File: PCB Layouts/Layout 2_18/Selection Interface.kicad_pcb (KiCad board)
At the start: 4 copper layers, 110 x 90 mm, 132 parts

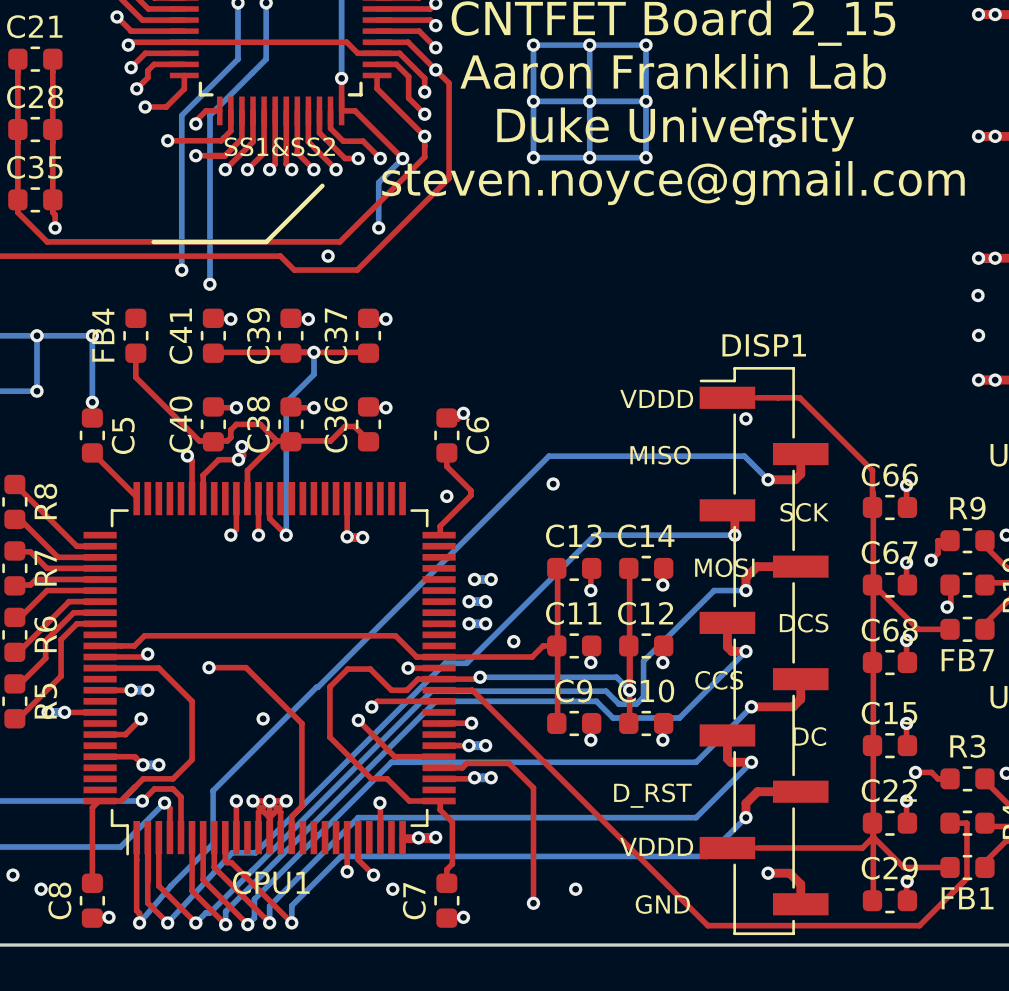
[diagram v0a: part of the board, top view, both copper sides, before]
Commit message: Removed display header from layout 2_18
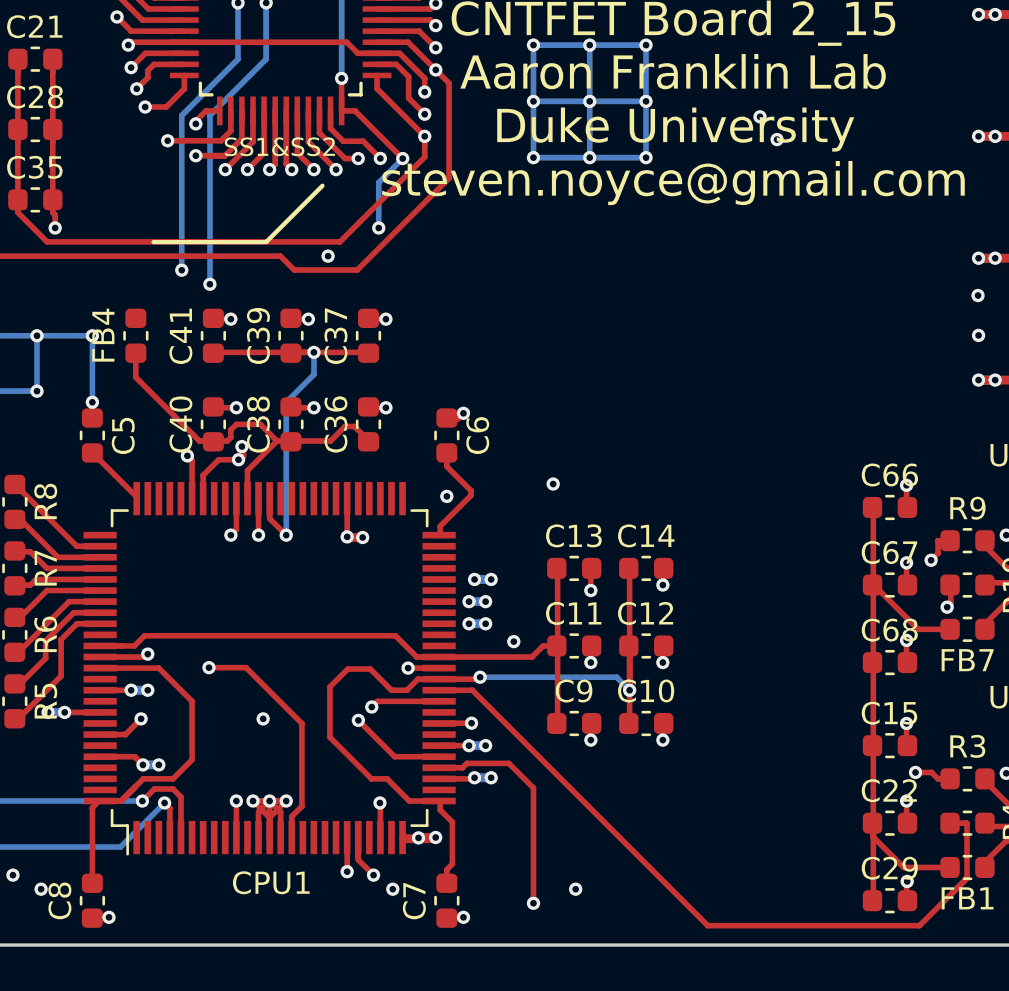
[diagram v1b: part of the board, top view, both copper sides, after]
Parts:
- removed DISP1: Conn_01x10, Connector_PinHeader_2.54mm:PinHeader_1x10_P2.54mm_Vertical_SMD_Pin1Left
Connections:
- CPU1 pad 1: DisplayMISO -> Net-(CPU1-Pad1)
- CPU1 pad 2: DisplaySCK -> Net-(CPU1-Pad2)
- CPU1 pad 3: DisplayMOSI -> Net-(CPU1-Pad3)
- CPU1 pad 6: DisplayCS -> Net-(CPU1-Pad6)
- CPU1 pad 7: CardCS -> Net-(CPU1-Pad7)
- CPU1 pad 8: DisplayDataOrCommand -> Net-(CPU1-Pad8)
- CPU1 pad 9: DisplayReset -> Net-(CPU1-Pad9)
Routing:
- net DisplayMISO: track 45.4 -> 0.00 mm, vias 2 -> 0
- net DisplaySCK: track 40.3 -> 0.00 mm, vias 2 -> 0
- net DisplayMOSI: track 40.3 -> 0.00 mm, vias 2 -> 0
- net DisplayCS: track 36.1 -> 0.00 mm, vias 2 -> 0
- net CardCS: track 35.3 -> 0.00 mm, vias 2 -> 0
- net DisplayDataOrCommand: track 32.2 -> 0.00 mm, vias 2 -> 0
- net DisplayReset: track 31.4 -> 0.00 mm, vias 2 -> 0
- net VDDD: track 281.8 -> 267.5 mm, vias 16 -> 15
- net GND: track 597.7 -> 595.2 mm, vias 189 -> 188
- net SolutionGate_Socket: track 94.1 -> 95.5 mm
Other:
- board text removed: "CCS"
- board text removed: "DC"
- board text removed: "DCS"
- board text removed: "D_RST"
- board text removed: "MISO"
- board text removed: "MOSI"
- board text removed: "SCK"

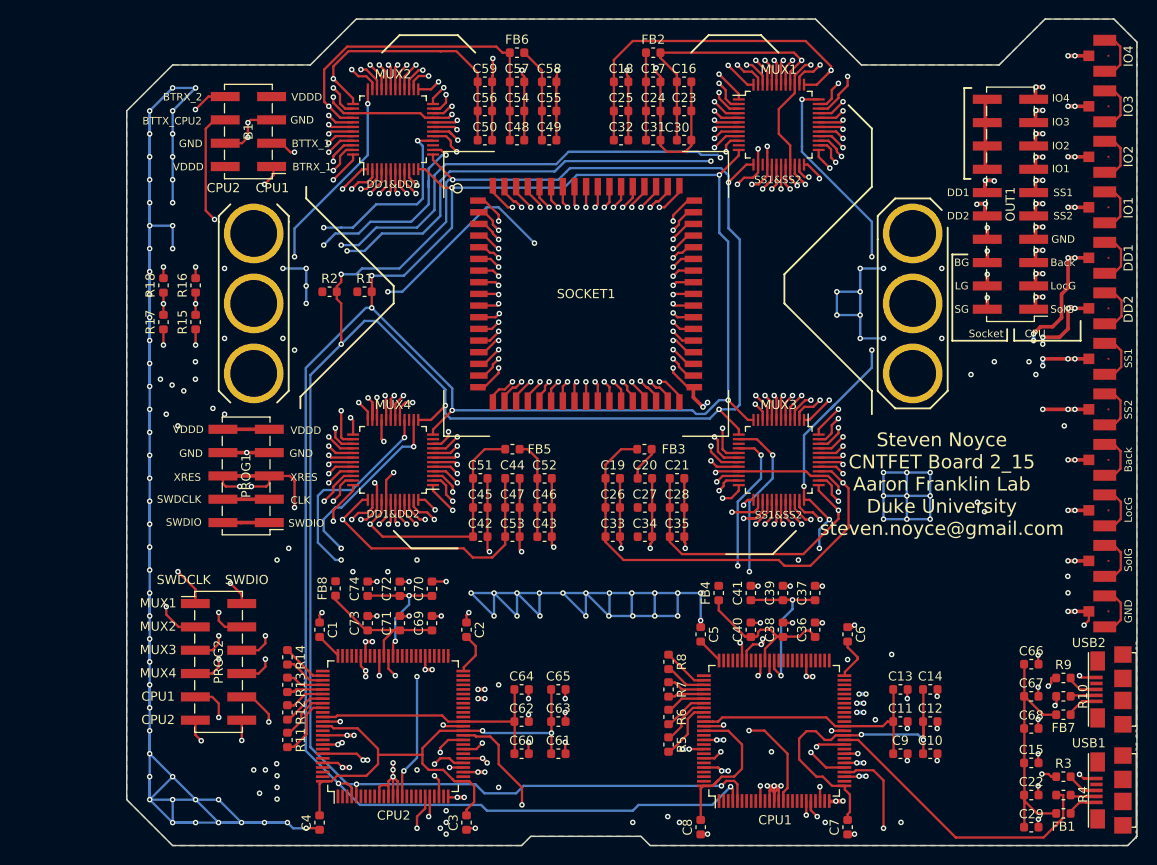
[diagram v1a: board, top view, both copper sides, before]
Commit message: Removed secondary master processor (CPU2) from Layout 2_18
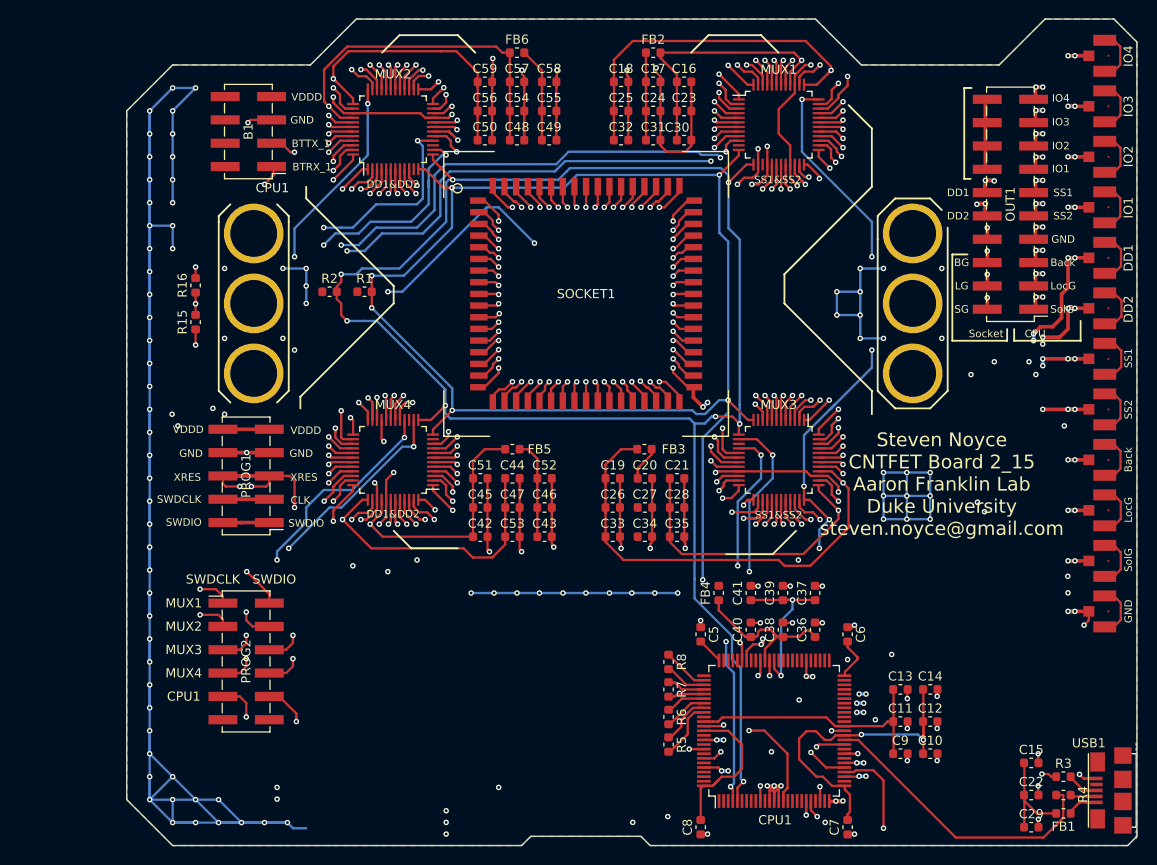
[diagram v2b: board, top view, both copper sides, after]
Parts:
- removed C1, C2, C3, C4, C64, C65, C68, C73, C74: 0.1uF, Capacitor_SMD:C_0603_1608Metric
- removed C60, C61, C66, C69, C70: 47uF, Capacitor_SMD:C_0603_1608Metric
- removed C62, C63, C67, C71, C72: 1uF, Capacitor_SMD:C_0603_1608Metric
- removed CPU2: CY8C58_(100_TQFP), Package_QFP:TQFP-100_14x14mm_P0.5mm
- removed FB7, FB8, R11, R12, R13, R14: R, Resistor_SMD:R_0603_1608Metric
- removed R10, R9: 22R, Resistor_SMD:R_0603_1608Metric
- removed R17: 1k, Resistor_SMD:R_0603_1608Metric
- removed R18: 2k, Resistor_SMD:R_0603_1608Metric
- removed USB2: USB_2.0_B, Custom_Footprint_Library:Micro_USB_2.0_B_SMD(10118192-0001LF)
- moved PROG2 3.00 mm to (163.0, 139.9)
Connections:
- B1 pad 2: VDDD -> Net-(B1-Pad2)
- B1 pad 4: GND -> Net-(B1-Pad4)
- B1 pad 6: BT2_TX -> Net-(B1-Pad6)
- B1 pad 8: BT2_RXR -> Net-(B1-Pad8)
- PROG2 pad 11: SWDCLK6 -> Net-(PROG2-Pad11)
- PROG2 pad 12: SWDIO6 -> Net-(PROG2-Pad12)
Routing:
- net BT2_TX: track 105.1 -> 0.00 mm, vias 5 -> 0
- net GND: track 595.2 -> 493.4 mm, vias 188 -> 149
- net USBDP_C2: track 86.3 -> 0.00 mm, vias 3 -> 0
- net USBDM_C2: track 82.4 -> 0.00 mm, vias 4 -> 0
- net VDDD: track 267.5 -> 186.7 mm, vias 15 -> 13
- net BT2_RX: track 77.3 -> 0.00 mm, vias 4 -> 0
- net I2C0_SCL: track 240.2 -> 180.8 mm, vias 8 -> 9
- net I2C0_SDA: track 246.5 -> 188.2 mm
- net IO1: track 143.5 -> 89.9 mm, vias 8 -> 6
- net IO4: track 142.3 -> 96.3 mm, vias 8 -> 6
- net IO3: track 142.1 -> 96.2 mm, vias 7 -> 5
- net SS2: track 201.7 -> 157.1 mm, vias 12 -> 10
- net IO2: track 131.5 -> 87.1 mm, vias 9 -> 7
- net SS1: track 205.3 -> 161.6 mm, vias 14 -> 11
- net LocalGates: track 116.6 -> 73.1 mm, vias 7 -> 5
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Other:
- board text removed: "BTRX_2"
- board text removed: "BTTX_CPU2"
- board text removed: "CPU2"

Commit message: Removed four IPEX connectors (for all of the miscellaneous IO pins). Also moved the bluetooth connector much closer to the microcontroller
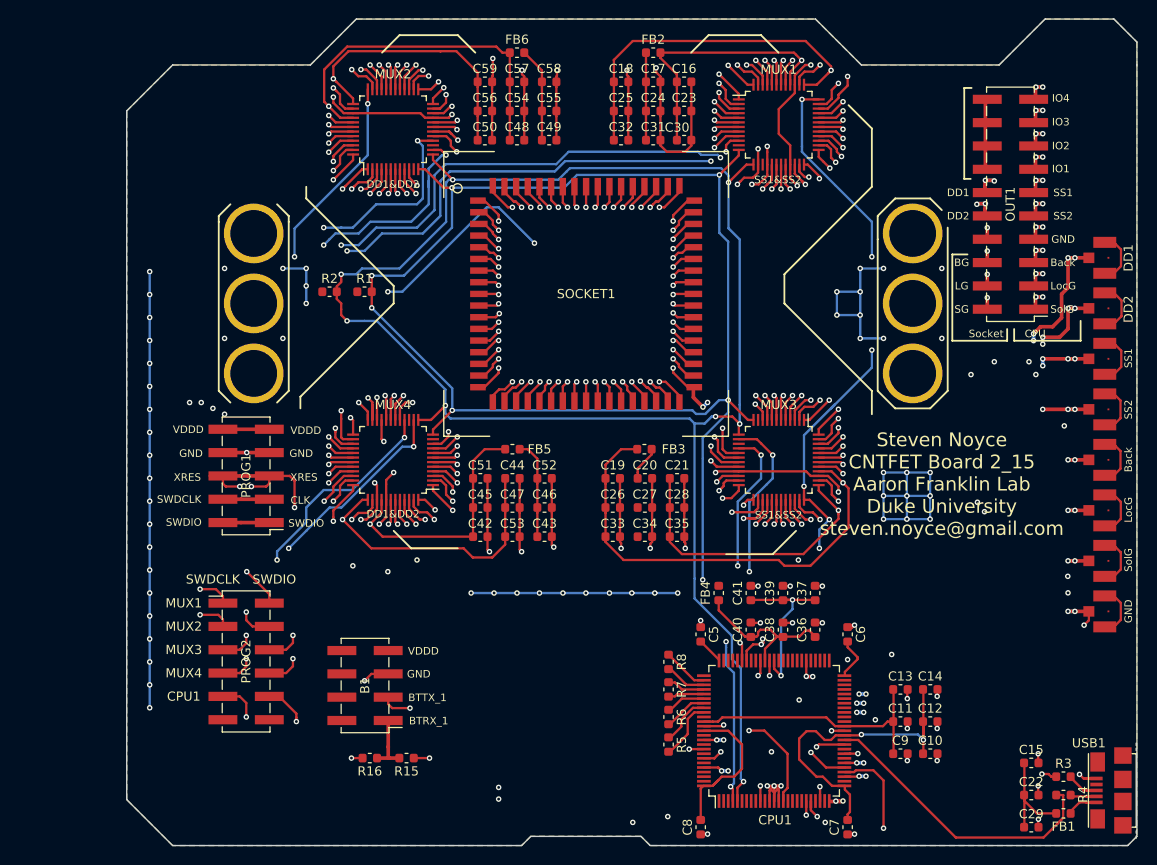
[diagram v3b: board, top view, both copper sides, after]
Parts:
- removed IPEX10, IPEX11, IPEX12, IPEX9: Conn_01x02, Custom_Footprint_Library:IPEX_Connector_SMD_(RECE.20279.001E.01)
- moved B1 61.6 mm to (175.9, 142.6)
- moved R16 54.9 mm to (176.5, 150.5), turned to 180 degrees
- moved R15 52.7 mm to (180.5, 150.5), turned to 180 degrees
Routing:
- net GND: track 493.4 -> 333.1 mm, vias 149 -> 119
- net BT1_TX: track 165.7 -> 68.4 mm, vias 6 -> 4
- net BT1_RX: track 139.4 -> 64.8 mm, vias 5 -> 3
- net BT1_RXR: track 24.6 -> 6.56 mm, vias 2 -> 0
- net IO1: track 89.9 -> 78.7 mm, vias 6 -> 4
- net IO4: track 96.3 -> 87.3 mm, vias 6 -> 4
- net IO3: track 96.2 -> 87.5 mm, vias 5 -> 3
- net IO2: track 87.1 -> 78.8 mm, vias 7 -> 5
- net Net-(IPEX11-Pad2): track 6.79 -> 0.00 mm
- net Net-(IPEX10-Pad2): track 6.79 -> 0.00 mm
- net Net-(IPEX9-Pad2): track 6.77 -> 0.00 mm
- net Net-(IPEX12-Pad2): track 6.76 -> 0.00 mm
- net SWDCLK2: track 88.0 -> 84.6 mm
- net SWDCLK1: track 122.8 -> 119.8 mm
- net SWDCLK5: track 76.9 -> 74.4 mm
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
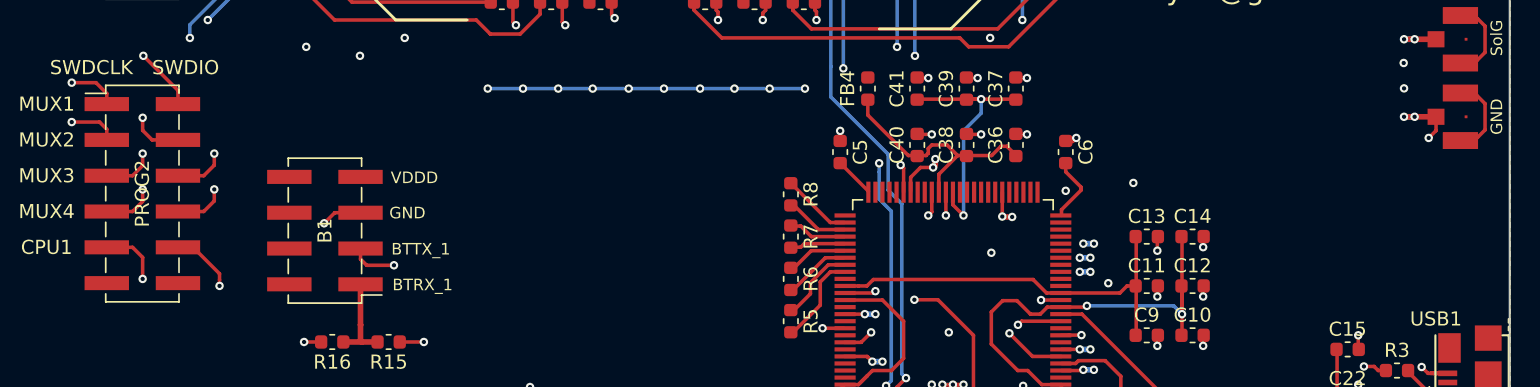
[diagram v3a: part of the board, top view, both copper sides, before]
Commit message: Removed the IPEX connection for GND, and got rid of some extra pins on the PROG2 header
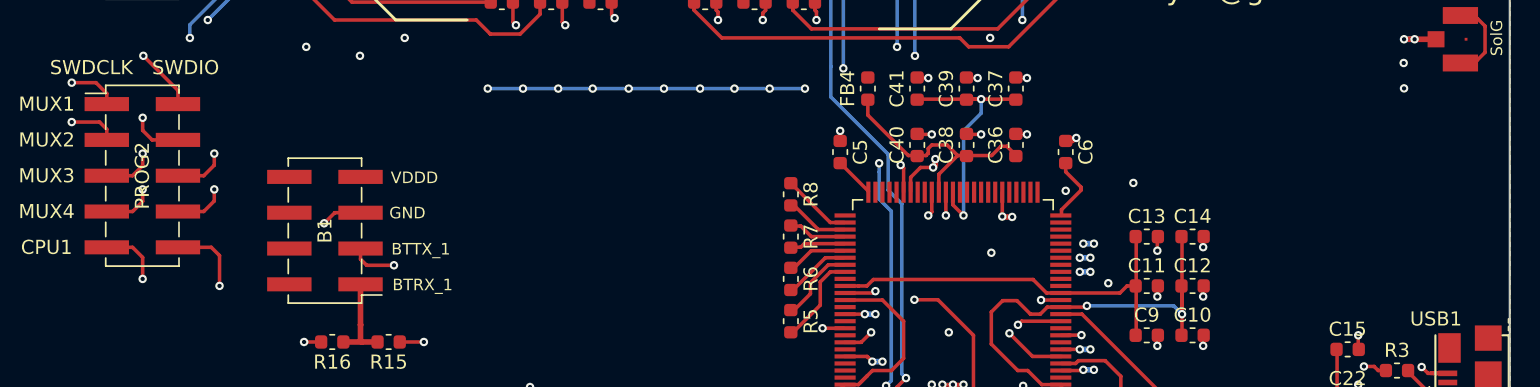
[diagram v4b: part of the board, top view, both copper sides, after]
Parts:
- removed IPEX1: Conn_01x02, Custom_Footprint_Library:IPEX_Connector_SMD_(RECE.20279.001E.01)
- PROG2: value Conn_02x06_Odd_Even -> Conn_02x05_Odd_Even; footprint Connector_PinHeader_2.54mm:PinHeader_2x06_P2.54mm_Vertical_SMD -> Connector_PinHeader_2.54mm:PinHeader_2x05_P2.54mm_Vertical_SMD
- moved PROG2 1.27 mm to (163.0, 138.7)
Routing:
- net Net-(IPEX1-Pad2): track 6.67 -> 0.00 mm
- net GND: track 333.1 -> 326.8 mm, vias 119 -> 116
- net SWDIO5: track 67.7 -> 68.4 mm

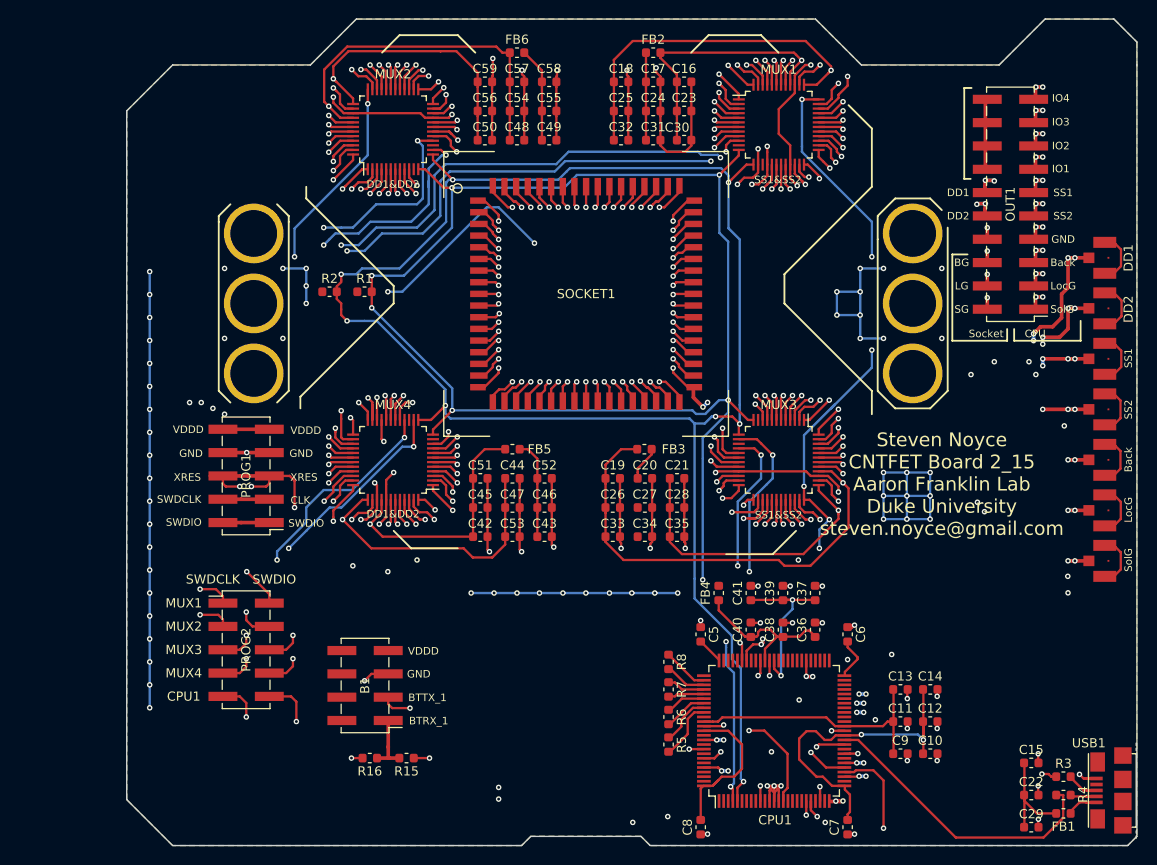
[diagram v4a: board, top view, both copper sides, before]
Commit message: Re-centered the remaining IPEX pins on the side of the PCB. Slightly trimmed the top corners of the PCB
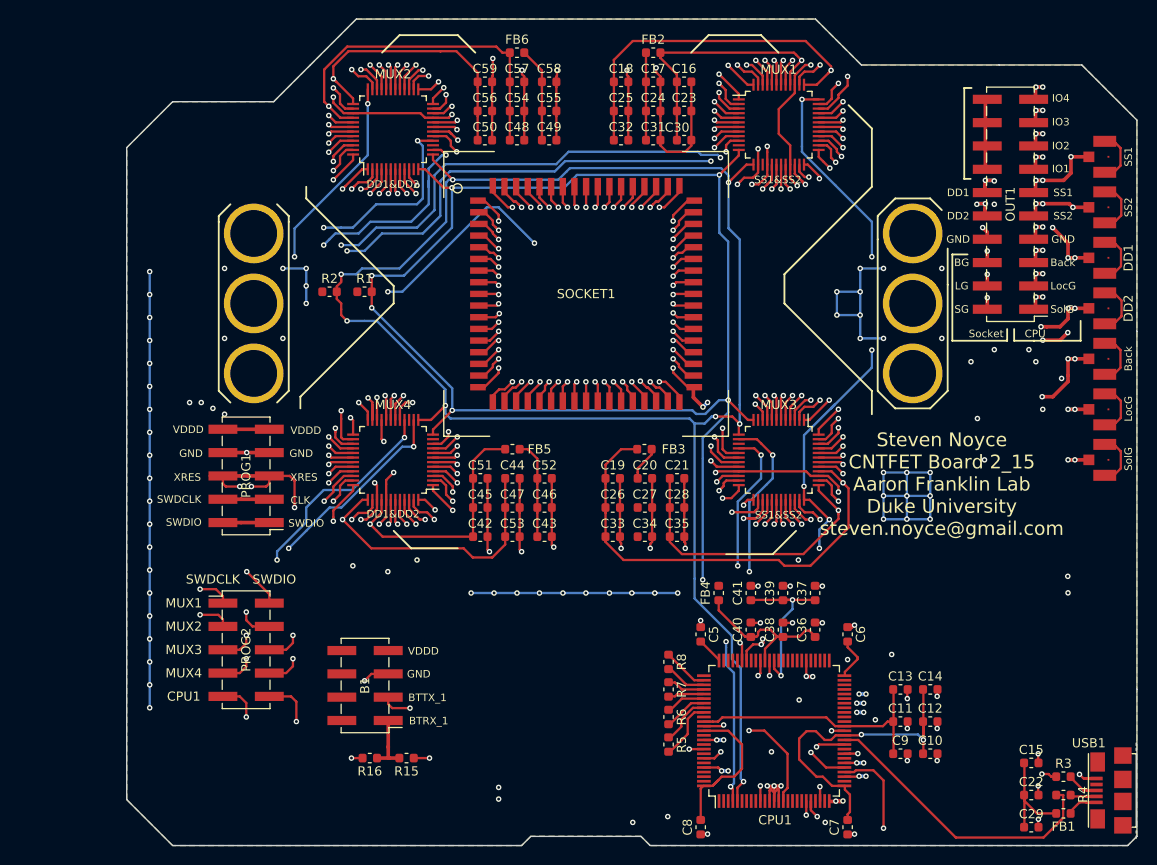
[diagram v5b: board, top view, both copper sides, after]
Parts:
- moved IPEX5 22.0 mm to (255.2, 90.5)
- moved IPEX6 22.0 mm to (255.2, 85.0)
- moved IPEX2 11.0 mm to (255.2, 118.0)
- moved IPEX3 11.0 mm to (255.2, 112.5)
- moved IPEX4 11.0 mm to (255.2, 107.0)
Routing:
- net SolutionGate_Socket: track 95.5 -> 83.9 mm
- net LocalGates_Socket: track 91.4 -> 82.3 mm
- net BackGate_Socket: track 79.7 -> 76.8 mm, vias 6 -> 7
- net DD1: track 265.4 -> 262.9 mm
- net SS1: track 161.6 -> 163.6 mm, vias 11 -> 10
- net DD2: track 265.1 -> 263.1 mm, vias 14 -> 13
- net SS2: track 157.1 -> 156.1 mm, vias 10 -> 9
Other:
- outline, holes or cut-outs redrawn
